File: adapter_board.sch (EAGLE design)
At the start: 29 parts, among them J1 62684-401100AHLF, J2 SFV6R-3STE1HLF, J3 54548-2271, U1 MAXIM_INTEGRATED-BOOST_CONVER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

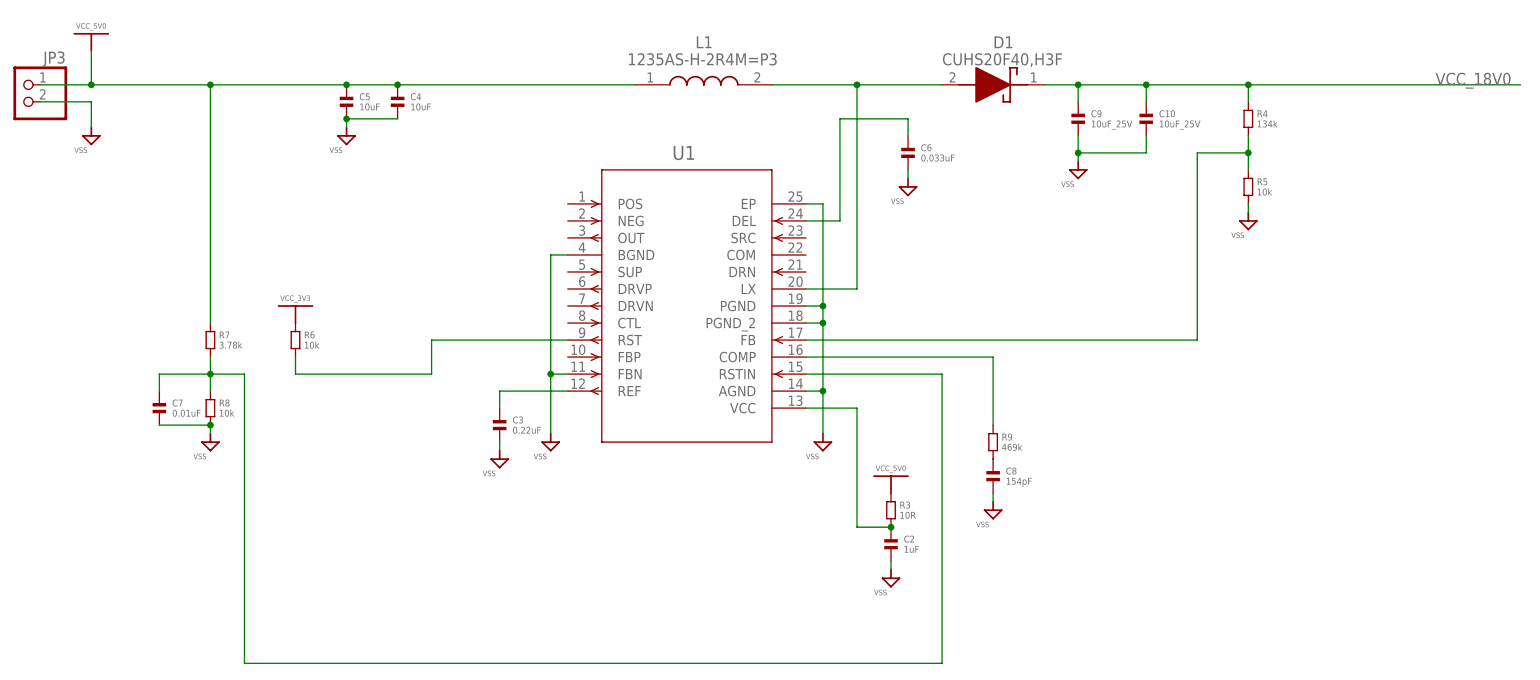
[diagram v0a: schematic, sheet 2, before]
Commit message: Finished backlight boost converter schematic
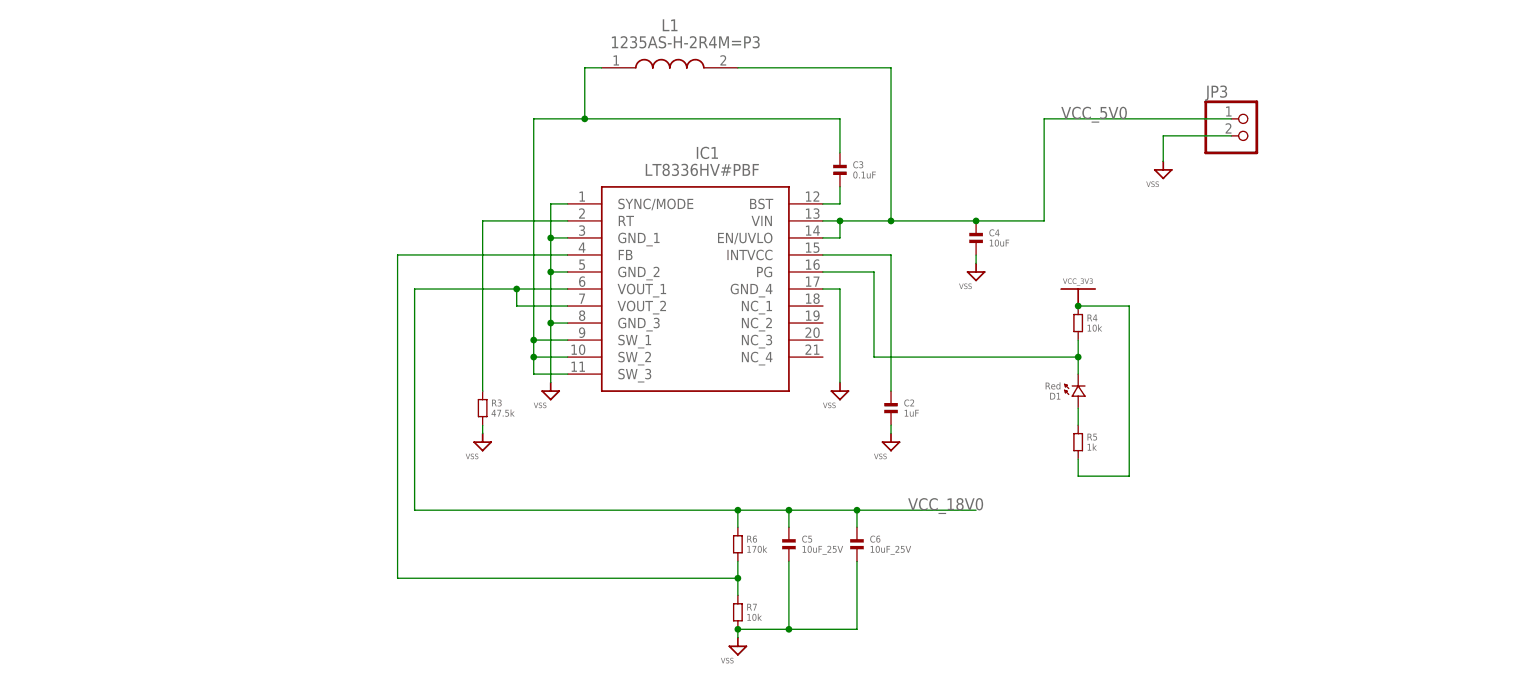
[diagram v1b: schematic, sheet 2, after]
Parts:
- removed C10, C9: 10uF_25V, standardparts:CAPACITOR.0805
- removed C7: 0.01uF, standardparts:CAPACITOR.0603
- removed C8: 154pF, standardparts:CAPACITOR.0603
- removed R8: 10k, standardparts:RESISTOR.0603
- removed R9: 469k, standardparts:RESISTOR.0603
- removed U1: MAXIM_INTEGRATED-BOOST_CONVERTER-MAX17075ETG+T, Module_Regulators:MAXIM_INTEGRATED-BOOST_CONVERTER-MAX17075ETG+T
- added IC1: LT8336HV#PBF, SamacSys_Parts:LT8336HV#PBF
- C3: value 0.22uF -> 0.1uF
- C5: value 10uF -> 10uF_25V; device standardparts:CAPACITOR.0603 -> standardparts:CAPACITOR.0805
- C6: value 0.033uF -> 10uF_25V; device standardparts:CAPACITOR.0603 -> standardparts:CAPACITOR.0805
- D1: value CUHS20F40,H3F -> Red; device SamacSys_Parts:CUHS20F40,H3F -> standardparts:LED.0603
- R3: value 10R -> 47.5k
- R4: value 134k -> 10k
- R5: value 10k -> 1k
- R6: value 10k -> 170k
- R7: value 3.78k -> 10k
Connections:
- removed net N$10: R6.2, U1.RST
- removed net N$11: C7.1, R7.2, R8.1, U1.RSTIN
- removed net N$5: C8.1, R9.2
- removed net N$6: C6.1, U1.DEL
- new net N$12: IC1.FB, R6.2, R7.1
- new net N$9: D1.1, R5.1
- net N$2: now also IC1.INTVCC; no longer R3.2, U1.VCC
- net N$3: now also IC1.RT, R3.1; no longer D1.A, L1.2, U1.LX
- net N$4: now also IC1.SW_1, IC1.SW_2, IC1.SW_3, L1.1; no longer U1.REF
- net N$7: now also C3.2, IC1.BST; no longer R4.2, R5.1, U1.FB
- net N$8: now also D1.2, IC1.PG, R4.2; no longer R9.1, U1.COMP
- net VCC_18V0: now also C5.1, C6.1, IC1.VOUT_1, IC1.VOUT_2, R6.1; no longer C10.1, C9.1, D1.K, R4.1
- net VCC_3V3: now also R4.1, R5.2; no longer R6.1
- net VCC_5V0: now also IC1.EN/UVLO, IC1.VIN, L1.2; no longer C5.1, L1.1, R3.1, R7.1
- net VSS: now also IC1.GND_1, IC1.GND_2, IC1.GND_3, IC1.GND_4, IC1.SYNC/MODE, R3.2, R7.2; no longer C10.2, C3.2, C7.2, C8.2, C9.2, R5.2, R8.2, U1.AGND, U1.BGND, U1.EP, U1.FBN, U1.PGND, U1.PGND_2
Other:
- moved on the sheet: C2, C3, C4, C5, C6, JP3, L1, R3, R4, R5, R6, R7

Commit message: Finished PCB. Generated fabrication data.
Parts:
- added C7: 0.1uF, standardparts:CAPACITOR.0603
- added R8: 330R, standardparts:RESISTOR.0603
- added TP1, TP2, TP3, TP4: (no value), microbuilder:TESTPOINTROUND1MM
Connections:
- new net N$5: R8.2, S7.1, S7.2
- net !RST: now also C7.1, R8.1; no longer S7.1, S7.2
- net N$8: now also TP2.P$1
- net VCC_18V0: now also TP1.P$1
- net VSS: now also C7.2, TP3.P$1, TP4.P$1
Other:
- moved on the sheet: S7

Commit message: Changed inductor L1.
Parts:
- L1: value 1235AS-H-2R4M=P3 -> SDR0603-2R5ML; device SamacSys_Parts:1235AS-H-2R4M=P3 -> SamacSys_Parts:SDR0603-2R5ML
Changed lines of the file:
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@@
 <part name="C5" library="standardparts" deviceset="CAPACITOR" device=".0805" value="10uF_25V"/>
 <part name="C6" library="standardparts" deviceset="CAPACITOR" device=".0805" value="10uF_25V"/>
-<part name="L1" library="SamacSys_Parts" deviceset="1235AS-H-2R4M=P3" device=""/>
 <part name="S19" library="Module_Supplies" deviceset="VSS" device=""/>
 <part name="JP3" library="pinhead" library_urn="urn:adsk.eagle:library:325" deviceset="PINHD-1X2" device="" package3d_urn="urn:adsk.eagle:package:22435/2"/>
@@
 <part name="TP3" library="microbuilder" deviceset="TESTPOINT" device="ROUND1MM"/>
 <part name="TP4" library="microbuilder" deviceset="TESTPOINT" device="ROUND1MM"/>
+<part name="L1" library="SamacSys_Parts" deviceset="SDR0603-2R5ML" device=""/>
 </parts>
 <sheets>
@@
 <attribute name="VALUE" x="27.305" y="-39.37" size="1.016" layer="96"/>
 </instance>
+<instance part="S19" gate="G$1" x="43.18" y="2.54" smashed="yes">
+<attribute name="VALUE" x="40.64" y="0" size="0.8128" layer="95"/>
+</instance>
+<instance part="JP3" gate="G$1" x="83.82" y="22.86" smashed="yes">
+<attribute name="NAME" x="77.47" y="28.575" size="1.778" layer="95"/>
+<attribute name="VALUE" x="77.47" y="17.78" size="1.778" layer="96"/>
+</instance>
+<instance part="S20" gate="G$1" x="71.12" y="17.78" smashed="yes">
+<attribute name="VALUE" x="68.58" y="15.24" size="0.8128" layer="95"/>
+</instance>
+<instance part="TP1" gate="G$1" x="0" y="-33.02" smashed="yes">
+<attribute name="NAME" x="-2.54" y="-25.4" size="1.27" layer="95"/>
+<attribute name="VALUE" x="-2.54" y="-27.305" size="1.27" layer="95"/>
+</instance>
+<instance part="TP2" gate="G$1" x="45.72" y="-10.16" smashed="yes">
+<attribute name="NAME" x="43.18" y="-2.54" size="1.27" layer="95"/>
+<attribute name="VALUE" x="43.18" y="-4.445" size="1.27" layer="95"/>
+</instance>
+<instance part="TP3" gate="G$1" x="43.18" y="-50.8" smashed="yes">
+<attribute name="NAME" x="40.64" y="-43.18" size="1.27" layer="95"/>
+<attribute name="VALUE" x="40.64" y="-45.085" size="1.27" layer="95"/>
+</instance>
+<instance part="TP4" gate="G$1" x="48.26" y="-50.8" smashed="yes">
+<attribute name="NAME" x="45.72" y="-43.18" size="1.27" layer="95"/>
+<attribute name="VALUE" x="45.72" y="-45.085" size="1.27" layer="95"/>
+</instance>
 <instance part="L1" gate="G$1" x="-12.7" y="33.02" smashed="yes">
 <attribute name="NAME" x="-3.81" y="39.37" size="1.778" layer="95" align="center-left"/>
 <attribute name="VALUE" x="-11.43" y="36.83" size="1.778" layer="96" align="center-left"/>
-</instance>
-<instance part="S19" gate="G$1" x="43.18" y="2.54" smashed="yes">
-<attribute name="VALUE" x="40.64" y="0" size="0.8128" layer="95"/>
-</instance>
-<instance part="JP3" gate="G$1" x="83.82" y="22.86" smashed="yes">
-<attribute name="NAME" x="77.47" y="28.575" size="1.778" layer="95"/>
-<attribute name="VALUE" x="77.47" y="17.78" size="1.778" layer="96"/>
-</instance>
-<instance part="S20" gate="G$1" x="71.12" y="17.78" smashed="yes">
-<attribute name="VALUE" x="68.58" y="15.24" size="0.8128" layer="95"/>
-</instance>
-<instance part="TP1" gate="G$1" x="0" y="-33.02" smashed="yes">
-<attribute name="NAME" x="-2.54" y="-25.4" size="1.27" layer="95"/>
-<attribute name="VALUE" x="-2.54" y="-27.305" size="1.27" layer="95"/>
-</instance>
-<instance part="TP2" gate="G$1" x="45.72" y="-10.16" smashed="yes">
-<attribute name="NAME" x="43.18" y="-2.54" size="1.27" layer="95"/>
-<attribute name="VALUE" x="43.18" y="-4.445" size="1.27" layer="95"/>
-</instance>
-<instance part="TP3" gate="G$1" x="43.18" y="-50.8" smashed="yes">
-<attribute name="NAME" x="40.64" y="-43.18" size="1.27" layer="95"/>
-<attribute name="VALUE" x="40.64" y="-45.085" size="1.27" layer="95"/>
-</instance>
-<instance part="TP4" gate="G$1" x="48.26" y="-50.8" smashed="yes">
-<attribute name="NAME" x="45.72" y="-43.18" size="1.27" layer="95"/>
-<attribute name="VALUE" x="45.72" y="-45.085" size="1.27" layer="95"/>
 </instance>
 </instances>
@@
 <wire x1="-15.24" y1="25.4" x2="22.86" y2="25.4" width="0.1524" layer="91"/>
 <wire x1="22.86" y1="25.4" x2="22.86" y2="20.32" width="0.1524" layer="91"/>
-<pinref part="L1" gate="G$1" pin="1"/>
 <wire x1="-12.7" y1="33.02" x2="-15.24" y2="33.02" width="0.1524" layer="91"/>
 <wire x1="-15.24" y1="33.02" x2="-15.24" y2="25.4" width="0.1524" layer="91"/>
 <junction x="-15.24" y="25.4"/>
+<pinref part="L1" gate="G$1" pin="1"/>
 </segment>
 </net>
@@
 <wire x1="22.86" y1="10.16" x2="30.48" y2="10.16" width="0.1524" layer="91"/>
 <junction x="22.86" y="10.16"/>
-<pinref part="L1" gate="G$1" pin="2"/>
 <wire x1="30.48" y1="10.16" x2="30.48" y2="33.02" width="0.1524" layer="91"/>
 <wire x1="30.48" y1="33.02" x2="7.62" y2="33.02" width="0.1524" layer="91"/>
@@
 <wire x1="53.34" y1="25.4" x2="81.28" y2="25.4" width="0.1524" layer="91"/>
 <label x="55.88" y="25.4" size="1.778" layer="95"/>
-</segment>
-</net>
+<pinref part="L1" gate="G$1" pin="2"/>
+</segment>
+</net>

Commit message: Changed PGOOD LED to 5V rail.
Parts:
- D1: value Red -> Green
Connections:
- net VCC_3V3: no longer R4.1, R5.2
- net VCC_5V0: now also R4.1, R5.2
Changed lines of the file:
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@@
 <part name="C4" library="standardparts" deviceset="CAPACITOR" device=".0603" value="10uF"/>
 <part name="R4" library="standardparts" deviceset="RESISTOR" device=".0603" value="10k"/>
-<part name="S17" library="Module_Supplies" deviceset="VCC_3V3" device=""/>
 <part name="R5" library="standardparts" deviceset="RESISTOR" device=".0603" value="1k"/>
-<part name="D1" library="standardparts" deviceset="LED" device=".0603" value="Red"/>
+<part name="D1" library="standardparts" deviceset="LED" device=".0603" value="Green"/>
 <part name="R6" library="standardparts" deviceset="RESISTOR" device=".0603" value="170k"/>
 <part name="R7" library="standardparts" deviceset="RESISTOR" device=".0603" value="10k"/>
@@
 <attribute name="VALUE" x="59.69" y="-6.35" size="1.016" layer="96"/>
 </instance>
-<instance part="S17" gate="G$1" x="58.42" y="-2.54" smashed="yes">
-<attribute name="VALUE" x="56.134" y="0.762" size="0.8128" layer="95"/>
-</instance>
 <instance part="R5" gate="G$1" x="58.42" y="-22.86" smashed="yes" rot="R270">
 <attribute name="NAME" x="59.69" y="-21.59" size="1.016" layer="95" rot="MR180"/>
@@
 <label x="55.88" y="25.4" size="1.778" layer="95"/>
 <pinref part="L1" gate="G$1" pin="2"/>
+<pinref part="R4" gate="G$1" pin="1"/>
+<pinref part="R5" gate="G$1" pin="2"/>
+<wire x1="58.42" y1="-25.4" x2="58.42" y2="-27.94" width="0.1524" layer="91"/>
+<wire x1="58.42" y1="-27.94" x2="66.04" y2="-27.94" width="0.1524" layer="91"/>
+<wire x1="66.04" y1="-27.94" x2="66.04" y2="-2.54" width="0.1524" layer="91"/>
+<wire x1="66.04" y1="-2.54" x2="58.42" y2="-2.54" width="0.1524" layer="91"/>
+<wire x1="58.42" y1="-2.54" x2="58.42" y2="10.16" width="0.1524" layer="91"/>
+<wire x1="58.42" y1="10.16" x2="53.34" y2="10.16" width="0.1524" layer="91"/>
+<junction x="58.42" y="-2.54"/>
+<junction x="53.34" y="10.16"/>
 </segment>
 </net>
@@
 </segment>
 </net>
-<net name="VCC_3V3" class="0">
-<segment>
-<pinref part="R4" gate="G$1" pin="1"/>
-<pinref part="S17" gate="G$1" pin="VCC_3V3"/>
-<pinref part="R5" gate="G$1" pin="2"/>
-<wire x1="58.42" y1="-25.4" x2="58.42" y2="-27.94" width="0.1524" layer="91"/>
-<wire x1="58.42" y1="-27.94" x2="66.04" y2="-27.94" width="0.1524" layer="91"/>
-<wire x1="66.04" y1="-27.94" x2="66.04" y2="-2.54" width="0.1524" layer="91"/>
-<wire x1="66.04" y1="-2.54" x2="58.42" y2="-2.54" width="0.1524" layer="91"/>
-<junction x="58.42" y="-2.54"/>
-</segment>
-</net>

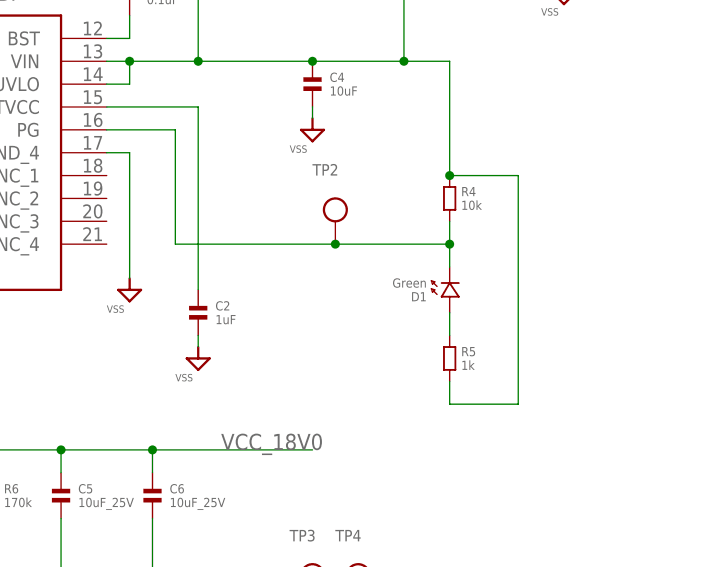
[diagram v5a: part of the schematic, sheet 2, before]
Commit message: Changed D1 back to red.
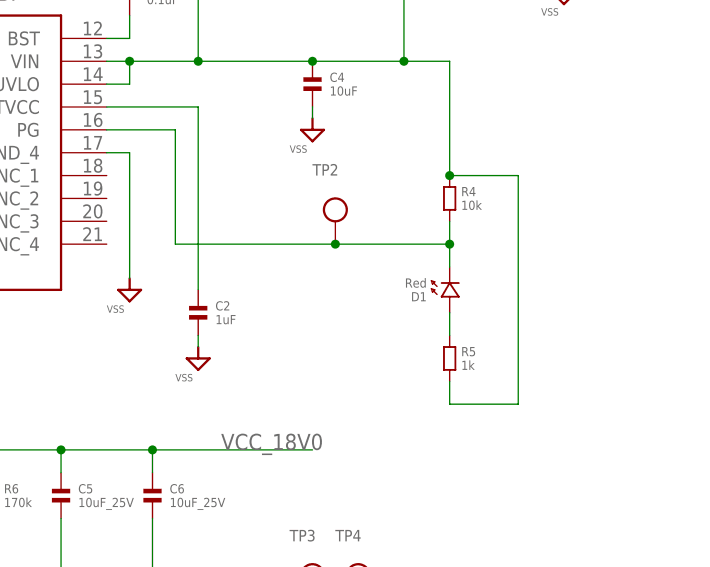
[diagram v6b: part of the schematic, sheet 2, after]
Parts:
- D1: value Green -> Red
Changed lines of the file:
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@@
 <part name="R4" library="standardparts" deviceset="RESISTOR" device=".0603" value="10k"/>
 <part name="R5" library="standardparts" deviceset="RESISTOR" device=".0603" value="1k"/>
-<part name="D1" library="standardparts" deviceset="LED" device=".0603" value="Green"/>
+<part name="D1" library="standardparts" deviceset="LED" device=".0603" value="Red"/>
 <part name="R6" library="standardparts" deviceset="RESISTOR" device=".0603" value="170k"/>
 <part name="R7" library="standardparts" deviceset="RESISTOR" device=".0603" value="10k"/>
